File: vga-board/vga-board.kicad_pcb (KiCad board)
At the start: 2 copper layers, 189.9 x 83.8 mm, 60 parts, among them J1 EXP, J2 EXP, J3 VGA, U1 GAL22V10, U10 74HC163, U11 74HC373, U12 74HC373, U13 74HC373, U14 74HC373, U15 74HC373, U16 74HC373, U17 74HC373, U18 74HC373, U19 74HC373, U2 74HC163, U20 74LS251, U21 74HC373, U22 74HC373, U23 74LS158, U24 74HC373, U25 74HC373, U3 74HC163, U4 74HC163, U5 71256SA12TPG, U6 GAL22V10, U7 GAL22V10, U8 74HC163, U9 74HC163, X1 40MHz

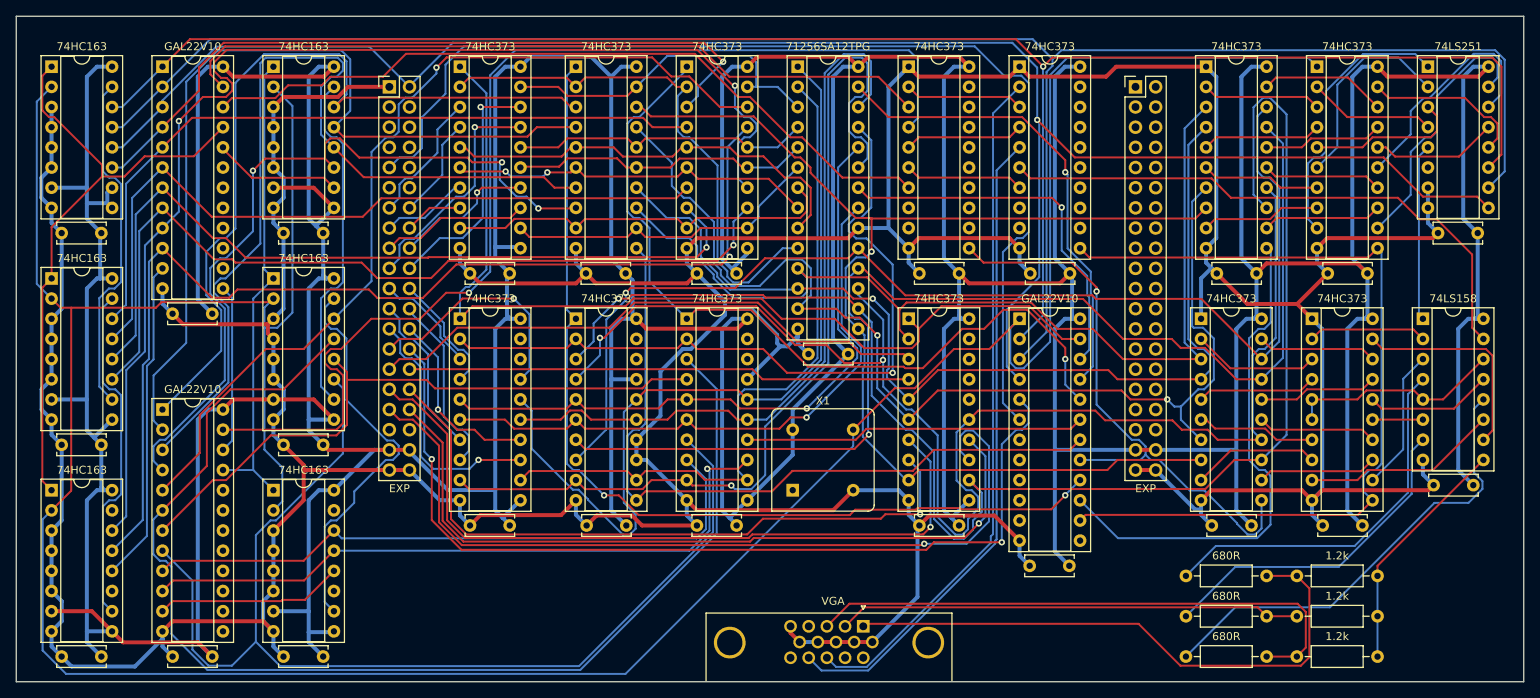
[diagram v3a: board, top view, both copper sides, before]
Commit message: Add sound board
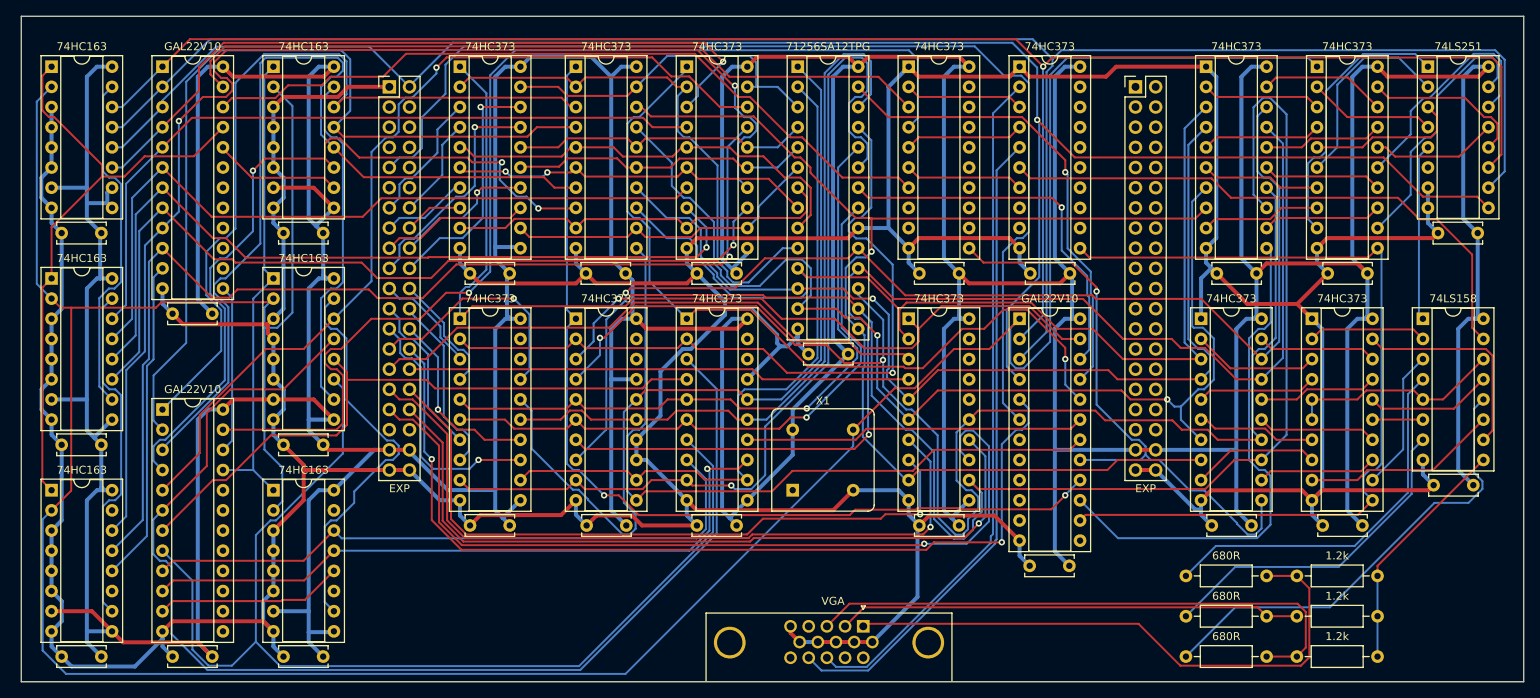
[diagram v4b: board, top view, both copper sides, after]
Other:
- board size 189.9 x 83.8 mm -> 189.2 x 83.8 mm

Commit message: route sound board
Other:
- board text added: "JLCJLCJLCJLC"

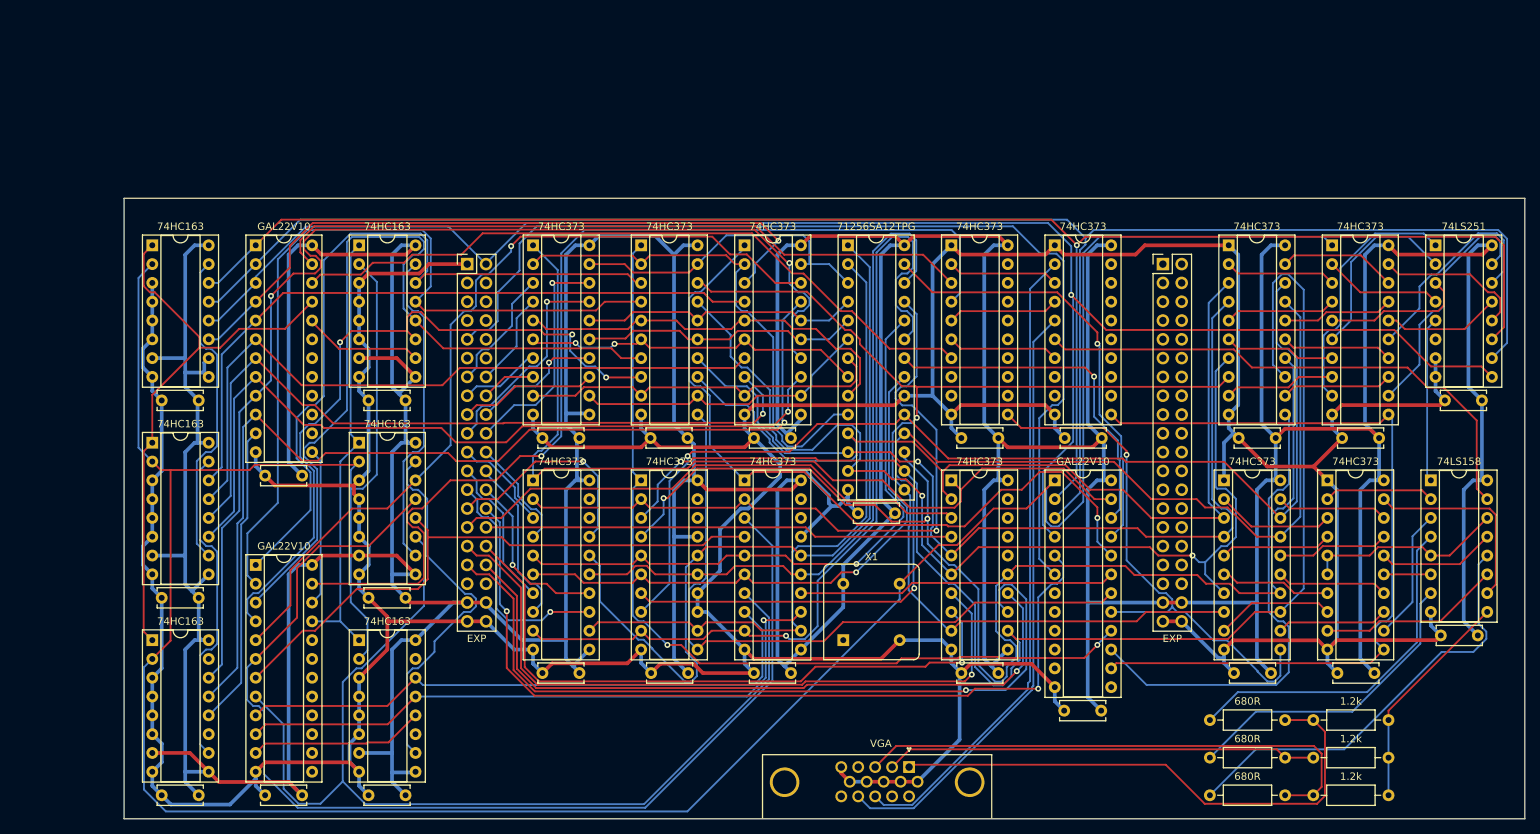
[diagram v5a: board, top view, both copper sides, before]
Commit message: remove old peripheral boards, begn new vga design
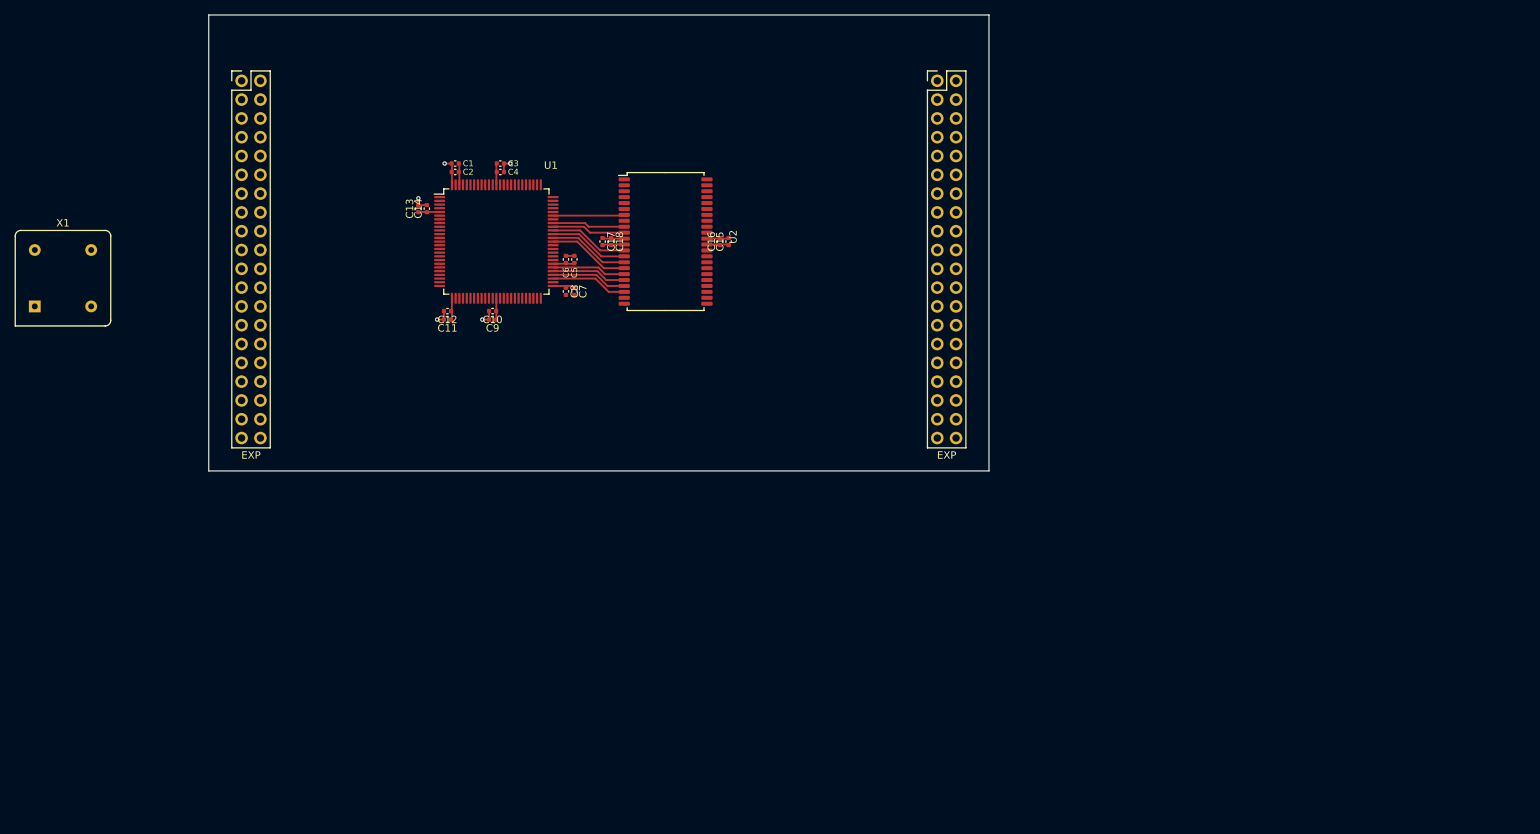
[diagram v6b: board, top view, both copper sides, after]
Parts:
- removed C19, C20, C21, C22, C23, C24, C25: 0.1uF, Capacitor_THT:C_Disc_D6.0mm_W2.5mm_P5.00mm
- removed J3: VGA, Connector_Dsub:DSUB-15-HD_Female_Horizontal_P2.29x1.98mm_EdgePinOffset3.03mm_Housed_MountingHolesOffset4.94mm
- removed R1, R3, R5: 680R, Resistor_THT:R_Axial_DIN0207_L6.3mm_D2.5mm_P10.16mm_Horizontal
- removed R2, R4, R6: 1.2k, Resistor_THT:R_Axial_DIN0207_L6.3mm_D2.5mm_P10.16mm_Horizontal
- removed U10, U3, U4, U8, U9: 74HC163, Package_DIP:DIP-16_W7.62mm_Socket
- removed U11, U12, U13, U14, U15, U16, U17, U18, U19, U21, U22, U24, U25: 74HC373, Package_DIP:DIP-20_W7.62mm_Socket
- removed U20: 74LS251, Package_DIP:DIP-16_W7.62mm_Socket
- removed U23: 74LS158, Package_DIP:DIP-16_W7.62mm_Socket
- removed U5: 71256SA12TPG, Package_DIP:DIP-28_W7.62mm_Socket
- removed U6, U7: GAL22V10, Package_DIP:DIP-24_W7.62mm_Socket
- C1, C11, C13, C15, C17, C3, C5, C7, C9: value 0.1uF -> 100n; footprint Capacitor_THT:C_Disc_D6.0mm_W2.5mm_P5.00mm -> Capacitor_SMD:C_0402_1005Metric
- C10, C12, C14, C16, C18, C2, C4, C6, C8: value 0.1uF -> 10n; footprint Capacitor_THT:C_Disc_D6.0mm_W2.5mm_P5.00mm -> Capacitor_SMD:C_0402_1005Metric
- U1: value GAL22V10 -> XC95144XL-TQ100; footprint Package_DIP:DIP-24_W7.62mm_Socket -> Package_QFP:TQFP-100_14x14mm_P0.5mm
- U2: value 74HC163 -> IS61C5128AL-10TLI; footprint Package_DIP:DIP-16_W7.62mm_Socket -> Package_SO:TSOP-II-44_10.16x18.41mm_P0.8mm
- X1: value 40MHz -> 50MHz
- moved C13 141.1 mm to (69.6, 83.3), turned to 90 degrees
- moved C9 135.0 mm to (79.6, 98.3), turned to 180 degrees
- moved C11 121.9 mm to (73.5, 98.3), turned to 180 degrees
- moved X1 118.2 mm to (17.8, 96.5)
- moved C4 95.8 mm to (80.7, 78.4)
- moved C3 91.1 mm to (80.7, 77.2)
- moved C16 74.9 mm to (110.4, 87.8), turned to 90 degrees
- moved C7 73.5 mm to (90.7, 94.5), turned to 270 degrees
- moved C2 69.9 mm to (74.6, 78.4), turned to 180 degrees
- moved U2 69.3 mm to (103.0, 87.8)
- moved C1 54.8 mm to (74.6, 77.2), turned to 180 degrees
- moved C6 50.0 mm to (89.5, 90.2), turned to 90 degrees
- moved C18 49.6 mm to (95.6, 87.8), turned to 270 degrees
- moved C10 49.4 mm to (79.6, 97.2), turned to 180 degrees
- moved C14 44.2 mm to (70.7, 83.3), turned to 90 degrees
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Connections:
- C1 pad 1: GND -> +3V3
- C1 pad 2: +5V -> GND
- C10 pad 1: GND -> +3V3
- C10 pad 2: +5V -> GND
- C11 pad 1: GND -> +3V3
- C11 pad 2: +5V -> GND
- C12 pad 1: GND -> +3V3
- C12 pad 2: +5V -> GND
- C13 pad 1: GND -> +3V3
- C13 pad 2: +5V -> GND
- C14 pad 1: GND -> +3V3
- C14 pad 2: +5V -> GND
- C15 pad 1: GND -> +3V3
- C15 pad 2: +5V -> GND
- C16 pad 1: GND -> +3V3
- C16 pad 2: +5V -> GND
- C17 pad 1: GND -> +3V3
- C17 pad 2: +5V -> GND
- C18 pad 1: GND -> +3V3
- C18 pad 2: +5V -> GND
- C2 pad 1: GND -> +3V3
- C2 pad 2: +5V -> GND
- C3 pad 1: GND -> +3V3
- C3 pad 2: +5V -> GND
- C4 pad 1: GND -> +3V3
- C4 pad 2: +5V -> GND
- C5 pad 1: GND -> +3V3
- C5 pad 2: +5V -> GND
- C6 pad 1: GND -> +3V3
- C6 pad 2: +5V -> GND
- C7 pad 1: GND -> +3V3
- C7 pad 2: +5V -> GND
- C8 pad 1: GND -> +3V3
- C8 pad 2: +5V -> GND
- C9 pad 1: GND -> +3V3
- C9 pad 2: +5V -> GND
- J1 pad 1: GND -> PHI1
- J1 pad 10: !RESET -> CLK
- J1 pad 11: RDY -> GND
- J1 pad 12: !P_SELECT -> GND
- J1 pad 2: CLK -> PHI2
- J1 pad 3: PHI1 -> !IRQ
- J1 pad 4: PHI2 -> !NMI
- J1 pad 5: !IRQ -> !READ
- J1 pad 6: !NMI -> !WRITE
- J1 pad 7: !READ -> R!W
- J1 pad 8: !WRITE -> !RESET
- J1 pad 9: R!W -> RDY
- J2 pad 37: +5V -> Net-(J2-Pad37)
- J2 pad 38: +5V -> Net-(J2-Pad38)
- J2 pad 39: GND -> Net-(J2-Pad39)
- J2 pad 40: GND -> Net-(J2-Pad40)
- U1 pad 1: X0 -> A0
- U1 pad 10: X9 -> Net-(U1-Pad10)
- U1 pad 11: X10 -> A8
- U1 pad 12: GND -> A9
- U1 pad 13: VBLANK -> A10
- U1 pad 14: Net-(U1-Pad14) -> A11
- U1 pad 15: Net-(U1-Pad15) -> A12
- U1 pad 16: Net-(U1-Pad16) -> A13
- U1 pad 17: Net-(U1-Pad17) -> A14
- U1 pad 18: Net-(U1-Pad18) -> A15
- U1 pad 2: X1 -> A1
- U1 pad 20: LINE_INC -> Net-(U1-Pad20)
- U1 pad 21: !HRST -> GND
- U1 pad 22: BLANK -> CLK_V
- U1 pad 23: HSYNC -> CLK
- U1 pad 24: +5V -> D0
- U1 pad 3: CLK -> A2
- U1 pad 4: X3 -> A3
- U1 pad 5: X4 -> +3V3
- U1 pad 6: X5 -> A4
- U1 pad 7: X6 -> A5
- U1 pad 8: X7 -> A6
- U1 pad 9: X8 -> A7
- U2 pad 1: !HRST -> Net-(U2-Pad1)
- U2 pad 10: +5V -> VD1
- U2 pad 11: X3 -> +3V3
- U2 pad 12: CLK -> GND
- U2 pad 13: X1 -> VD2
- U2 pad 14: X0 -> VD3
- U2 pad 15: Net-(U2-Pad15) -> VWE
- U2 pad 16: +5V -> VA5
- U2 pad 2: VCLK -> Net-(U2-Pad2)
- U2 pad 3: GND -> VA0
- U2 pad 4: GND -> VA1
- U2 pad 5: GND -> VA2
- U2 pad 6: GND -> VA3
- U2 pad 7: +5V -> VA4
- U2 pad 9: +5V -> VD0
- X1 pad 5: VCLK -> CLK_V
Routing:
- net +5V: track 1078.6 -> 0.00 mm
- net GND: track 733.4 -> 19.1 mm, vias 0 -> 5
- net VCLK: track 389.4 -> 0.00 mm
- net X1: track 238.5 -> 0.00 mm
- net CLK: track 231.1 -> 0.00 mm, vias 1 -> 0
- net X0: track 229.8 -> 0.00 mm, vias 1 -> 0
- net VD4: track 188.1 -> 0.00 mm, vias 1 -> 0
- net VD5: track 175.0 -> 0.00 mm, vias 2 -> 0
- net Y5: track 153.1 -> 0.00 mm
- net X8: track 152.7 -> 0.00 mm, vias 2 -> 0
- net VD6: track 151.3 -> 0.00 mm, vias 1 -> 0
- net VD7: track 146.6 -> 0.00 mm, vias 1 -> 0
- net VD3: track 155.0 -> 10.9 mm, vias 1 -> 0
- net Y7: track 141.4 -> 0.00 mm
- net VSYNC: track 140.0 -> 0.00 mm, vias 1 -> 0
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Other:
- board size 189.2 x 83.8 mm -> 105.4 x 61.6 mm
- net class Default: via_dia 0.8 -> 0.6; via_drill 0.4 -> 0.3
- net class Wide removed

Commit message: continue new vga
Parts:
- added J3: Conn_02x05_Odd_Even, Connector_IDC:IDC-Header_2x05_P2.54mm_Vertical, F.Cu at (74.3, 109.9)
- moved C7 0.25 mm to (90.7, 94.2)
- moved C8 0.25 mm to (89.5, 94.2)
- moved C5 0.13 mm to (90.7, 90.0)
- moved C6 0.13 mm to (89.5, 90.0)
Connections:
- U1 pad 45: Net-(U1-Pad45) -> TDI
- U1 pad 47: Net-(U1-Pad47) -> TMS
- U1 pad 48: Net-(U1-Pad48) -> TCK
- U1 pad 83: Net-(U1-Pad83) -> TDO
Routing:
- net VA10: track 0.00 -> 33.5 mm
- net VA11: track 0.00 -> 32.9 mm
- net VA12: track 0.00 -> 32.2 mm
- net VA13: track 0.00 -> 31.6 mm
- net VA18: track 0.00 -> 31.2 mm
- net VA17: track 0.00 -> 30.5 mm
- net VA16: track 0.00 -> 29.9 mm
- net VA14: track 0.00 -> 29.8 mm
- net VA15: track 0.00 -> 29.3 mm
- net VOE: track 0.00 -> 28.7 mm
- net VD7: track 0.00 -> 28.1 mm
- net VD4: track 0.00 -> 27.7 mm
- net VD6: track 0.00 -> 27.4 mm
- net VD5: track 0.00 -> 27.1 mm
- net +3V3: track 26.6 -> 44.7 mm
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
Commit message: more vga board routing
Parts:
- added C19: 100n, Capacitor_SMD:C_0402_1005Metric, F.Cu at (71.1, 111.1)
- added C20: 10n, Capacitor_SMD:C_0402_1005Metric, F.Cu at (71.1, 109.9)
- added J4: DB15_Female_HighDensity, Connector_Dsub:DSUB-15-HD_Female_Horizontal_P2.29x1.98mm_EdgePinOffset3.03mm_Housed_MountingHolesOffset4.94mm, F.Cu at (67.9, 54.6)
- added R1: 560R, Resistor_SMD:R_0402_1005Metric, F.Cu at (64.1, 69.2)
- added R10: 560R, Resistor_SMD:R_0402_1005Metric, F.Cu at (67.9, 64.1)
- added R11: 560R, Resistor_SMD:R_0402_1005Metric, F.Cu at (67.9, 66.7)
- added R12: 560R, Resistor_SMD:R_0402_1005Metric, F.Cu at (69.2, 66.7)
- added R13: 47R, Resistor_SMD:R_0402_1005Metric, F.Cu at (70.5, 64.1)
- added R14: 560R, Resistor_SMD:R_0402_1005Metric, F.Cu at (69.2, 64.1)
- added R15: 560R, Resistor_SMD:R_0402_1005Metric, F.Cu at (71.8, 69.2)
- added R16: 560R, Resistor_SMD:R_0402_1005Metric, F.Cu at (73.0, 69.2)
- added R17: 560R, Resistor_SMD:R_0402_1005Metric, F.Cu at (71.8, 64.1)
- added R18: 560R, Resistor_SMD:R_0402_1005Metric, F.Cu at (71.8, 66.7)
- added R19: 560R, Resistor_SMD:R_0402_1005Metric, F.Cu at (73.0, 66.7)
- added R2: 560R, Resistor_SMD:R_0402_1005Metric, F.Cu at (65.4, 69.2)
- added R20: 47R, Resistor_SMD:R_0402_1005Metric, F.Cu at (74.3, 64.1)
- added R21: 560R, Resistor_SMD:R_0402_1005Metric, F.Cu at (73.0, 64.1)
- added R3: 560R, Resistor_SMD:R_0402_1005Metric, F.Cu at (64.1, 64.1)
- added R4: 560R, Resistor_SMD:R_0402_1005Metric, F.Cu at (64.1, 66.7)
- added R5: 560R, Resistor_SMD:R_0402_1005Metric, F.Cu at (65.4, 66.7)
- added R6: 560R, Resistor_SMD:R_0402_1005Metric, F.Cu at (65.4, 64.1)
- added R7: 47R, Resistor_SMD:R_0402_1005Metric, F.Cu at (66.7, 64.1)
- added R8: 560R, Resistor_SMD:R_0402_1005Metric, F.Cu at (67.9, 69.2)
- added R9: 560R, Resistor_SMD:R_0402_1005Metric, F.Cu at (69.2, 69.2)
- X1: value 50MHz -> ABLNO; footprint Oscillator:Oscillator_DIP-8 -> Oscillator:Oscillator_SMD_Abracon_ASV-4Pin_7.0x5.1mm
- moved J3 64.2 mm to (104.8, 53.3)
- moved X1 54.1 mm to (71.1, 105.4)
- moved C13 9.63 mm to (60.1, 81.9)
- moved C14 9.63 mm to (61.2, 81.9)
- moved C1 8.98 mm to (65.7, 75.9)
- moved C2 8.98 mm to (65.7, 77.1)
- moved C15 8.35 mm to (103.3, 86.5)
- moved C16 8.35 mm to (102.1, 86.5)
- moved C17 8.35 mm to (86.2, 86.5)
- moved C18 8.35 mm to (87.4, 86.5)
- moved C5 8.35 mm to (82.4, 88.8)
- moved C6 8.35 mm to (81.3, 88.8)
- moved U1 8.35 mm to (71.9, 86.5)
- moved U2 8.35 mm to (94.7, 86.5)
- moved C12 8.35 mm to (65.3, 95.9)
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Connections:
- U1 pad 1: A0 -> !RESET
- U1 pad 10: Net-(U1-Pad10) -> A6
- U1 pad 11: A8 -> A7
- U1 pad 12: A9 -> A8
- U1 pad 13: A10 -> A9
- U1 pad 14: A11 -> A10
- U1 pad 15: A12 -> A11
- U1 pad 16: A13 -> A12
- U1 pad 17: A14 -> A13
- U1 pad 18: A15 -> A14
- U1 pad 19: Net-(U1-Pad19) -> A15
- U1 pad 2: A1 -> R!W
- U1 pad 20: Net-(U1-Pad20) -> D0
- U1 pad 22: CLK_V -> D1
- U1 pad 24: D0 -> D3
- U1 pad 25: D1 -> D2
- U1 pad 27: D2 -> CLK_V
- U1 pad 28: D3 -> D5
- U1 pad 3: A2 -> A0
- U1 pad 30: D5 -> D7
- U1 pad 33: D7 -> Net-(U1-Pad33)
- U1 pad 4: A3 -> A1
- U1 pad 6: A4 -> A2
- U1 pad 7: A5 -> A3
- U1 pad 8: A6 -> A4
- U1 pad 9: A7 -> A5
- U1 pad 90: Net-(U1-Pad90) -> HSYNC
- U1 pad 91: Net-(U1-Pad91) -> VSYNC
- U1 pad 92: Net-(U1-Pad92) -> B0
- U1 pad 93: Net-(U1-Pad93) -> B1
- U1 pad 94: Net-(U1-Pad94) -> G0
- U1 pad 95: Net-(U1-Pad95) -> G1
- U1 pad 96: Net-(U1-Pad96) -> R0
- U1 pad 97: Net-(U1-Pad97) -> R1
- X1 pad 1: Net-(X1-Pad1) -> +3V3
- X1 pad 4: GND -> +3V3
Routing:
- net CLK: track 0.00 -> 53.1 mm
- net HSYNC: track 0.00 -> 39.3 mm
- net VSYNC: track 0.00 -> 36.1 mm
- net D6: track 0.00 -> 32.0 mm
- net D4: track 0.00 -> 29.6 mm
- net D7: track 0.00 -> 27.7 mm
- net D5: track 0.00 -> 25.5 mm
- net D2: track 0.00 -> 24.3 mm
- net D0: track 0.00 -> 23.3 mm
- net A14: track 0.00 -> 22.7 mm
- net A12: track 0.00 -> 22.0 mm
- net R!W: track 0.00 -> 21.5 mm
- net A10: track 0.00 -> 21.4 mm
- net D3: track 0.00 -> 21.0 mm
- net A8: track 0.00 -> 20.8 mm
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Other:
- board size 105.4 x 61.6 mm -> 105.4 x 71.8 mm
